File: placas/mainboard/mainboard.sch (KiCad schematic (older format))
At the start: 58 parts, among them IC1 DRV8843, K1 OjitoC1, K2 OjitoC2, K3 OjitoB1, K4 OjitoB2, K5 OjitoA1, K6 OjitoA2, P1 Bateria, P2 MI, P3 MD, P4 CONN_3X2, P5 CONN_3X2, P6 Solenoide, Q1 NPN, Q2 NPN, Q3 NPN, Q4 NPN, SW1 SW_PUSH_SMALL, U1 REG_104-5, U2 MBED

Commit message: transicion
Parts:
- added C? (x3): 4.7u, symbol CP
- added R? (x3): 100, symbol R
- C11, C12, C13: value 10u -> 4.7u
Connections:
- wire segments 255 -> 273
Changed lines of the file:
@@
-EESchema Schematic File Version 2  date jue 25 ago 2011 16:27:50 ART
+EESchema Schematic File Version 2  date jue 25 ago 2011 20:51:28 ART
 LIBS:power
 LIBS:device
@@
 $EndDescr
 Wire Wire Line
+	8850 2350 8450 2350
+Connection ~ 9900 1300
+Wire Wire Line
+	9900 1300 10350 1300
+Wire Wire Line
+	10350 1300 10350 1250
+Connection ~ 9900 700
+Wire Wire Line
+	9650 750  9650 700
+Wire Wire Line
+	9650 700  10100 700
+Wire Wire Line
+	9900 1250 9900 1600
+Connection ~ 9800 3100
+Wire Wire Line
+	9800 3100 10250 3100
+Wire Wire Line
+	10250 3100 10250 3050
+Wire Wire Line
+	9550 3400 9550 3050
+Connection ~ 9450 5100
+Wire Wire Line
+	9450 5100 10150 5100
+Wire Wire Line
+	10150 5100 10150 5200
+Connection ~ 9700 5600
+Wire Wire Line
+	9450 5550 9450 5600
+Wire Wire Line
+	9450 5600 9700 5600
+Wire Wire Line
+	9450 4800 9450 5150
+Wire Wire Line
 	6600 1250 6300 1250
 Wire Wire Line
@@
 	6600 2850 6300 2850
 Wire Wire Line
-	8750 2350 8450 2350
-Wire Wire Line
 	8750 1850 8450 1850
 Wire Wire Line
@@
 	8750 1250 8450 1250
 Wire Wire Line
-	850  5100 850  5250
+	850  5250 850  5100
 Wire Wire Line
 	3800 2250 4200 2250
@@
 Connection ~ 1450 1700
 Wire Wire Line
-	1450 1700 1450 1650
+	1450 1650 1450 1700
 Wire Wire Line
 	2300 1700 2300 2300
@@
 	9700 5650 9700 5550
 Wire Wire Line
-	9700 4800 9700 5150
-Wire Wire Line
-	9700 4300 9700 4250
-Wire Wire Line
-	9700 4250 9900 4250
-Wire Wire Line
-	9900 4250 9900 4300
+	9700 5150 9700 4800
+Wire Wire Line
+	9700 4250 9700 4300
+Wire Wire Line
+	9900 4300 9900 4250
 Wire Wire Line
 	9900 5400 10250 5400
 Connection ~ 9900 5000
 Wire Wire Line
-	10250 5200 10150 5200
+	10150 5200 10250 5200
 Connection ~ 10200 5300
 Wire Wire Line
@@
 Connection ~ 9800 4250
 Wire Wire Line
-	10150 5050 9700 5050
-Connection ~ 9700 5050
-Connection ~ 10150 5050
-Wire Wire Line
 	10200 4900 10200 5650
 Wire Wire Line
-	9250 5000 10250 5000
-Wire Wire Line
-	10150 4800 10150 5200
-Wire Wire Line
-	10250 3050 10250 3450
-Wire Wire Line
-	10350 3250 9350 3250
+	10250 5000 9050 5000
+Wire Wire Line
+	9150 3250 10350 3250
 Wire Wire Line
 	10300 3900 10300 3150
-Connection ~ 10250 3300
-Connection ~ 9800 3300
-Wire Wire Line
-	9800 3300 10250 3300
 Connection ~ 9900 2500
 Wire Wire Line
@@
 Connection ~ 10300 3550
 Wire Wire Line
-	10250 3450 10350 3450
+	10350 3450 10250 3450
 Connection ~ 10000 3250
 Wire Wire Line
@@
 Wire Wire Line
 	10000 2550 10000 2500
-Wire Wire Line
-	10000 2500 9800 2500
 Wire Wire Line
 	9800 2500 9800 2550
@@
 	9900 2100 9900 2000
 Wire Wire Line
-	9900 1250 9900 1600
-Wire Wire Line
-	9900 750  9900 700
-Wire Wire Line
-	10100 750  10100 700
+	9900 700  9900 750
+Wire Wire Line
+	10100 700  10100 750
 Wire Wire Line
 	10100 1850 10450 1850
@@
 Connection ~ 7650 5250
 Wire Wire Line
-	7650 5250 7650 5850
+	7650 5850 7650 5250
 Connection ~ 6500 4200
 Wire Wire Line
@@
 	6600 1550 6200 1550
 Wire Wire Line
-	800  3200 1150 3200
+	1150 3200 800  3200
 Wire Wire Line
 	3750 1550 4200 1550
@@
 	7050 4200 7050 4100
 Wire Wire Line
-	7550 5200 7550 5250
+	7550 5250 7550 5200
 Wire Wire Line
 	6100 5250 6100 5200
@@
 	7350 4200 7350 4250
 Wire Wire Line
-	6300 4200 6300 4250
+	6300 4250 6300 4200
 Wire Wire Line
 	3950 7350 3600 7350
@@
 Connection ~ 850  5150
 Wire Wire Line
-	850  5150 1400 5150
+	1400 5150 850  5150
 Connection ~ 850  6050
 Wire Wire Line
@@
 Connection ~ 4750 6400
 Wire Wire Line
-	4750 6500 4750 5250
-Wire Wire Line
-	3300 6400 4750 6400
-Wire Wire Line
-	4750 5600 3300 5600
+	4750 5250 4750 6500
+Wire Wire Line
+	4750 6400 3300 6400
+Wire Wire Line
+	3300 5600 4750 5600
 Wire Wire Line
 	4600 5150 4600 5250
@@
 	3950 7550 3600 7550
 Wire Wire Line
-	7550 4250 7550 4200
+	7550 4200 7550 4250
 Connection ~ 7550 4200
 Wire Wire Line
-	6300 5200 6300 5250
+	6300 5250 6300 5200
 Wire Wire Line
 	7350 5250 7350 5200
@@
 	8450 2150 8850 2150
 Wire Wire Line
-	1350 3400 1350 3750
-Wire Wire Line
-	10450 1250 10350 1250
+	1350 3750 1350 3400
+Wire Wire Line
+	10350 1250 10450 1250
 Wire Wire Line
 	4150 1350 4200 1350
@@
 	7300 5400 6800 5400
 Wire Wire Line
-	6400 5250 6400 5850
+	6400 5850 6400 5250
 Connection ~ 6400 5250
 Wire Wire Line
-	10000 700  10000 650
+	10000 650  10000 700
 Connection ~ 10000 700
 Wire Wire Line
-	10350 1500 9900 1500
-Connection ~ 9900 1500
-Connection ~ 10350 1500
-Wire Wire Line
 	10400 1350 10400 2100
 Wire Wire Line
-	9450 1450 10450 1450
+	10450 1450 9250 1450
 Wire Wire Line
 	2850 3800 2800 3800
@@
 Connection ~ 7050 4200
 Wire Wire Line
-	10350 1250 10350 1650
-Wire Wire Line
 	9200 6300 9550 6300
 Wire Wire Line
@@
 	8750 1050 8450 1050
 Wire Wire Line
-	10100 700  9900 700
-Wire Wire Line
 	8450 1150 8750 1150
 Wire Wire Line
@@
 Wire Wire Line
 	8450 1950 8750 1950
+Wire Wire Line
+	9450 4300 9450 4250
+Wire Wire Line
+	9450 4250 9900 4250
+Connection ~ 9700 4250
+Wire Wire Line
+	10150 4800 10150 4900
+Wire Wire Line
+	10150 4900 9700 4900
+Connection ~ 9700 4900
+Wire Wire Line
+	10000 2500 9550 2500
+Wire Wire Line
+	9550 2500 9550 2550
+Connection ~ 9800 2500
+Wire Wire Line
+	9800 3850 9550 3850
+Wire Wire Line
+	9550 3850 9550 3800
+Connection ~ 9800 3850
+Wire Wire Line
+	10250 3450 10250 3350
+Wire Wire Line
+	10250 3350 9550 3350
+Connection ~ 9550 3350
+Wire Wire Line
+	9650 2000 9650 2050
+Wire Wire Line
+	9650 2050 9900 2050
+Connection ~ 9900 2050
+Wire Wire Line
+	9650 1250 9650 1600
+Wire Wire Line
+	10350 1650 10350 1550
+Wire Wire Line
+	10350 1550 9650 1550
+Connection ~ 9650 1550
+$Comp
+L R R?
+U 1 1 4E56B7B3
+P 9650 1000
+F 0 "R?" V 9730 1000 50  0000 C CNN
+F 1 "100" V 9650 1000 50  0000 C CNN
+	1    9650 1000
+	1    0    0    -1
+$EndComp
+$Comp
+L CP C?
+U 1 1 4E56B7AB
+P 9650 1800
+F 0 "C?" H 9700 1900 50  0000 L CNN
+F 1 "4.7u" H 9700 1700 50  0000 L CNN
+	1    9650 1800
+	-1   0    0    -1
+$EndComp
+$Comp
+L R R?
+U 1 1 4E56B700
+P 9550 2800
+F 0 "R?" V 9630 2800 50  0000 C CNN
+F 1 "100" V 9550 2800 50  0000 C CNN
+	1    9550 2800
+	1    0    0    -1
+$EndComp
+$Comp
+L CP C?
+U 1 1 4E56B6FC
+P 9550 3600
+F 0 "C?" H 9600 3700 50  0000 L CNN
+F 1 "4.7u" H 9600 3500 50  0000 L CNN
+	1    9550 3600
+	-1   0    0    -1
+$EndComp
+$Comp
+L CP C?
+U 1 1 4E56B686
+P 9450 5350
+F 0 "C?" H 9500 5450 50  0000 L CNN
+F 1 "4.7u" H 9500 5250 50  0000 L CNN
+	1    9450 5350
+	-1   0    0    -1
+$EndComp
+$Comp
+L R R?
+U 1 1 4E56B682
+P 9450 4550
+F 0 "R?" V 9530 4550 50  0000 C CNN
+F 1 "100" V 9450 4550 50  0000 C CNN
+	1    9450 4550
+	1    0    0    -1
+$EndComp
 Text Label 8750 1050 2    60   ~ 0
 3v3
@@
 	1    0    0    1
 $EndComp
-Text Label 9250 5000 0    60   ~ 0
+Text Label 9050 5000 0    60   ~ 0
 OjitoC
 $Comp
@@
 P 9700 5350
 F 0 "C11" H 9750 5450 50  0000 L CNN
-F 1 "10u" H 9750 5250 50  0000 L CNN
+F 1 "4.7u" H 9750 5250 50  0000 L CNN
 	1    9700 5350
-	-1   0    0    -1
+	1    0    0    -1
 $EndComp
 $Comp
@@
 P 9800 3600
 F 0 "C12" H 9850 3700 50  0000 L CNN
-F 1 "10u" H 9850 3500 50  0000 L CNN
+F 1 "4.7u" H 9850 3500 50  0000 L CNN
 	1    9800 3600
-	-1   0    0    -1
+	1    0    0    -1
 $EndComp
 $Comp
@@
 	1    0    0    -1
 $EndComp
-Text Label 9350 3250 0    60   ~ 0
+Text Label 9150 3250 0    60   ~ 0
 OjitoB
-Text Label 9450 1450 0    60   ~ 0
+Text Label 9250 1450 0    60   ~ 0
 OjitoA
 Text Label 1900 3800 0    60   ~ 0
@@
 Text Label 8950 2850 2    60   ~ 0
 OjitosEmit1
-Text Label 6250 2250 0    60   ~ 0
+Text Label 8850 2050 2    60   ~ 0
 Puls
 Text Label 6200 1750 0    60   ~ 0
@@
 	1    0    0    -1
 $EndComp
-Text Label 8850 2050 2    60   ~ 0
+Text Label 8850 2150 2    60   ~ 0
 nReset
-Text Label 8850 2150 2    60   ~ 0
+Text Label 8850 2250 2    60   ~ 0
 nSleep
-Text Label 8850 2250 2    60   ~ 0
+Text Label 8850 2350 2    60   ~ 0
 nFault
 Text Label 8900 2750 2    60   ~ 0
@@
 P 9900 1800
 F 0 "C13" H 9950 1900 50  0000 L CNN
-F 1 "10u" H 9950 1700 50  0000 L CNN
+F 1 "4.7u" H 9950 1700 50  0000 L CNN
 	1    9900 1800
-	-1   0    0    -1
-$EndComp
-$Comp
+	1    0    0    -1
+$EndComp
+$Comp

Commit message: placa principal terminada
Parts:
- gave numbers to parts that had none: 6
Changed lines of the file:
@@
-EESchema Schematic File Version 2  date jue 25 ago 2011 20:51:28 ART
+EESchema Schematic File Version 2  date jue 25 ago 2011 20:52:22 ART
 LIBS:power
 LIBS:device
@@
 Connection ~ 9650 1550
 $Comp
-L R R?
+L R R6
 U 1 1 4E56B7B3
 P 9650 1000
-F 0 "R?" V 9730 1000 50  0000 C CNN
+F 0 "R6" V 9730 1000 50  0000 C CNN
 F 1 "100" V 9650 1000 50  0000 C CNN
 	1    9650 1000
@@
 $EndComp
 $Comp
-L CP C?
+L CP C16
 U 1 1 4E56B7AB
 P 9650 1800
-F 0 "C?" H 9700 1900 50  0000 L CNN
+F 0 "C16" H 9700 1900 50  0000 L CNN
 F 1 "4.7u" H 9700 1700 50  0000 L CNN
 	1    9650 1800
@@
 $EndComp
 $Comp
-L R R?
+L R R5
 U 1 1 4E56B700
 P 9550 2800
-F 0 "R?" V 9630 2800 50  0000 C CNN
+F 0 "R5" V 9630 2800 50  0000 C CNN
 F 1 "100" V 9550 2800 50  0000 C CNN
 	1    9550 2800
@@
 $EndComp
 $Comp
-L CP C?
+L CP C15
 U 1 1 4E56B6FC
 P 9550 3600
-F 0 "C?" H 9600 3700 50  0000 L CNN
+F 0 "C15" H 9600 3700 50  0000 L CNN
 F 1 "4.7u" H 9600 3500 50  0000 L CNN
 	1    9550 3600
@@
 $EndComp
 $Comp
-L CP C?
+L CP C14
 U 1 1 4E56B686
 P 9450 5350
-F 0 "C?" H 9500 5450 50  0000 L CNN
+F 0 "C14" H 9500 5450 50  0000 L CNN
 F 1 "4.7u" H 9500 5250 50  0000 L CNN
 	1    9450 5350
@@
 $EndComp
 $Comp
-L R R?
+L R R4
 U 1 1 4E56B682
 P 9450 4550
-F 0 "R?" V 9530 4550 50  0000 C CNN
+F 0 "R4" V 9530 4550 50  0000 C CNN
 F 1 "100" V 9450 4550 50  0000 C CNN
 	1    9450 4550

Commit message: retoques finales
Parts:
- added P7: CONN_1, symbol CONN_1
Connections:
- wire segments 273 -> 275

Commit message: cambios en el puente h, reubicacion de componentes en la placa
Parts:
- removed C1: 100n, symbol C
- removed IC1: DRV8843, HTSSOP28, symbol DRV8843
- removed R1, R2: 10k, symbol R
- added C1: 2.2u, symbol CP
- added IC1: DRV8833, symbol DRV8833
- added JP1: JUMPER, symbol JUMPER
- added P8: CONN_1, symbol CONN_1
- C9: value 100u -> 10u
- R10, R11, R13, R14, R15, R9: value 220 -> 2k2
- R12, R8: value 1k -> 10k
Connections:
- net labels removed: nReset
- wire segments 275 -> 236
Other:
- moved on the sheet: C10, C7, C8, C9, P2, P3, P4, P5, P7, Q1, R3

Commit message: nueva version de la placa mainboard
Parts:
- removed C11, C12, C13, C14, C15: 4.7u, symbol CP
- removed D2, D3, D4, D5: LED, symbol LED
- removed K1: OjitoC1, symbol CONN_3
- removed K2: OjitoC2, symbol CONN_3
- removed K3: OjitoB1, symbol CONN_3
- removed K4: OjitoB2, symbol CONN_3
- removed K5: OjitoA1, symbol CONN_3
- removed R10, R11, R13, R14: 2k2, symbol R
- removed R17, R18, R19, R4, R5: 100, symbol R
- removed R20, R21: 4.7k, symbol R
- added C_OJ2: 4.7u, symbol CP
- added C_UC1: 100n, symbol C
- added IC_UC1: ATMEGA88PA-P, DIL28, symbol ATMEGA88PA-P
- added K_OJ2: OjitoATR, symbol CONN_3
- added P1, P2: CONN_1, symbol CONN_1
- added P_UC1: CONN_3X2, symbol CONN_3X2
- added P_UC2: CONN_4, symbol CONN_4
- added R_OJ4: 4.7k, symbol R
- added R_OJ8: 100, symbol R
- added R_UC1: 10k, symbol R
- added SW_UC1: SW_PUSH_SMALL, symbol SW_PUSH_SMALL
- K_OJ1: renamed from K6; value OjitoA2 -> OjitoAD
- renumbered C2 to C_B1, C4 to C_B2, C5 to C_B3, C6 to C_B4, C16 to C_OJ1, C8 to C_PH1, C1 to C_PH2, C7 to C_PH3, C9 to C_PH4, C10 to C_PH5, C3 to C_Pl1, D1 to D_OJ1, D6 to D_OJ2, D7 to D_SL1, IC1 to IC_PH1, U2 to IC_UC2, JP1 to JP_B1, P7 to P3, P8 to P4, P1 to P_B1, P4 to P_E1, P5 to P_E2, P2 to P_PH1, P3 to P_PH2, P6 to P_SL1, Q1 to Q_E1, Q2 to Q_OJ1, Q3 to Q_OJ2, Q4 to Q_SL1, R3 to R_E1, R8 to R_OJ1, R9 to R_OJ2, R22 to R_OJ3, R15 to R_OJ5, R12 to R_OJ6, R6 to R_OJ7, R16 to R_SL1, SW1 to SW_Pl1, U1 to U_B1
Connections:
- net labels added: ATMISO, ATMOSI, ATRESET, ATRX, ATSCK, ATTX, OjitoRecepAd, OjitoRecepAtr, OjitosEmitAd, OjitosEmitAtr
- net labels removed: OjitoA, OjitoB, OjitoC, OjitosEmit1, OjitosEmit2
- wire segments 236 -> 238
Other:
- moved on the sheet: C_OJ1, D_OJ1, D_OJ2, D_SL1, K_OJ1, P3, P_PH1, P_PH2, P_SL1, Q_OJ1, Q_OJ2, Q_SL1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

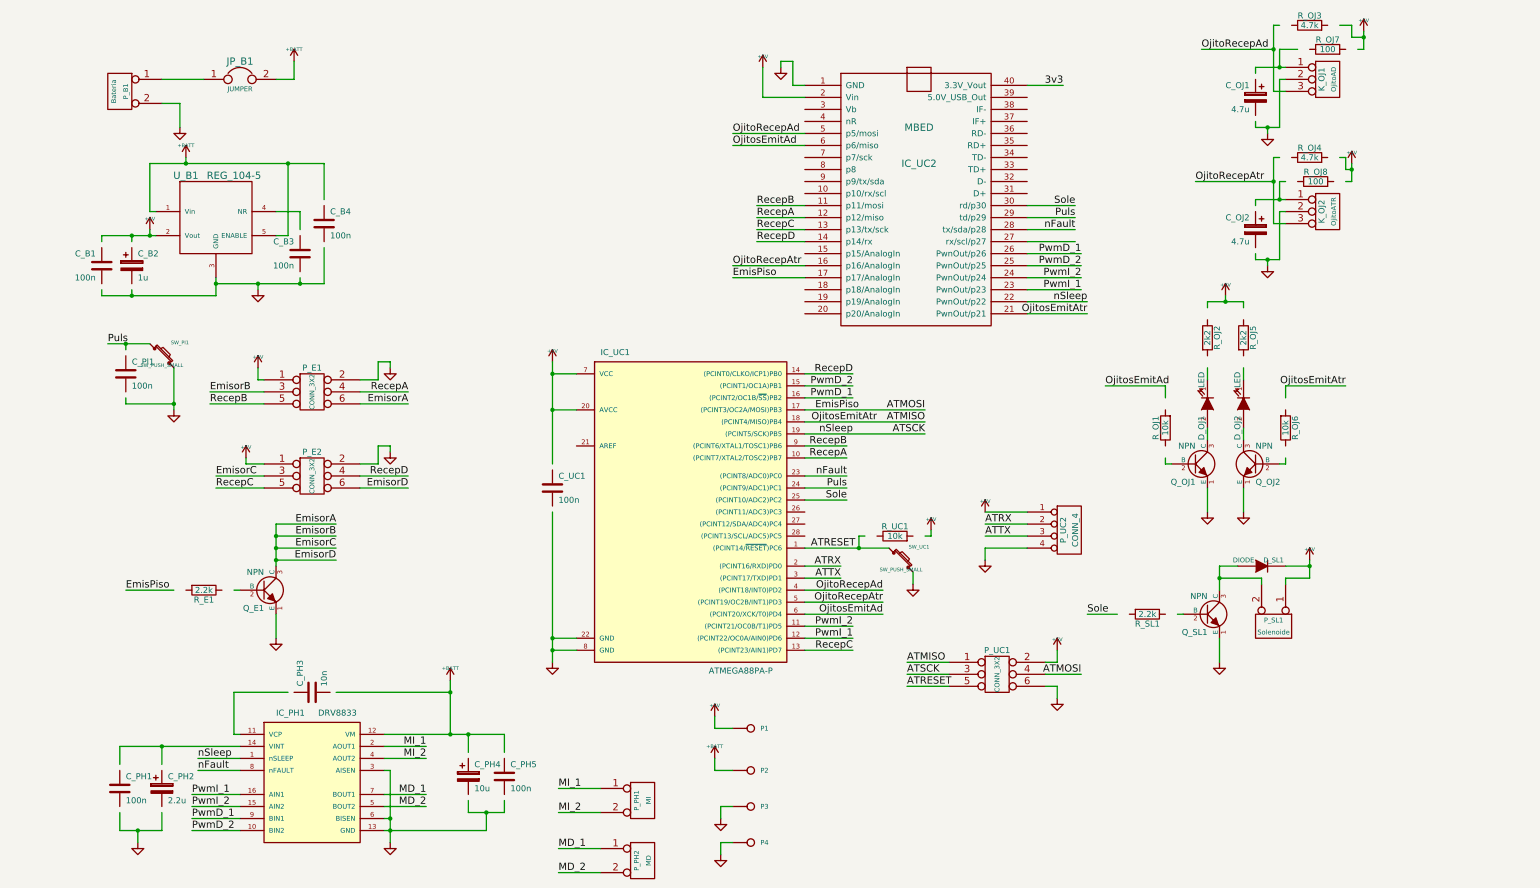
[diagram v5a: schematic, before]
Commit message: reposicionamos un receptor del piso y eliminamos el receptor infrarrojo trasero
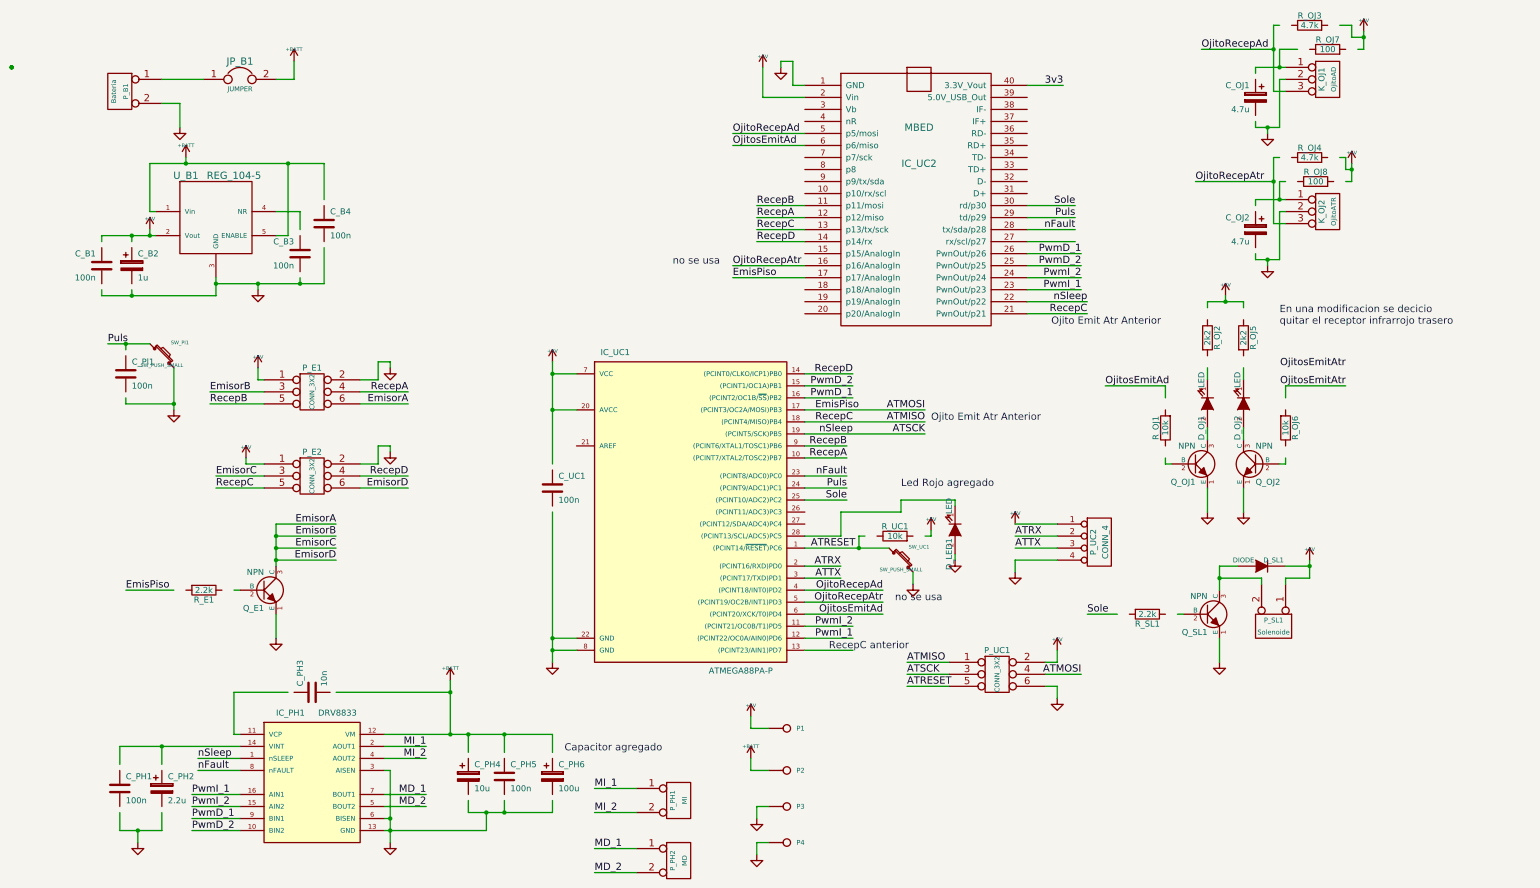
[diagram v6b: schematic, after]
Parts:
- added C_PH6: 100u, symbol CP
- added D_LED1: LED, symbol LED
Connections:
- wire segments 238 -> 247
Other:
- note added: "Capacitor agregado"
- note added: "En una modificacion se decicio\nquitar el receptor infrarrojo trasero"
- note added: "Led Rojo agregado"
- note added: "Ojito Emit Atr Anterior"
- note added: "RecepC anterior"
- note added: "no se usa"
- moved on the sheet: P1, P2, P3, P4, P_PH1, P_PH2, P_UC2

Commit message: actualizo las placas con las modificaciones hechas
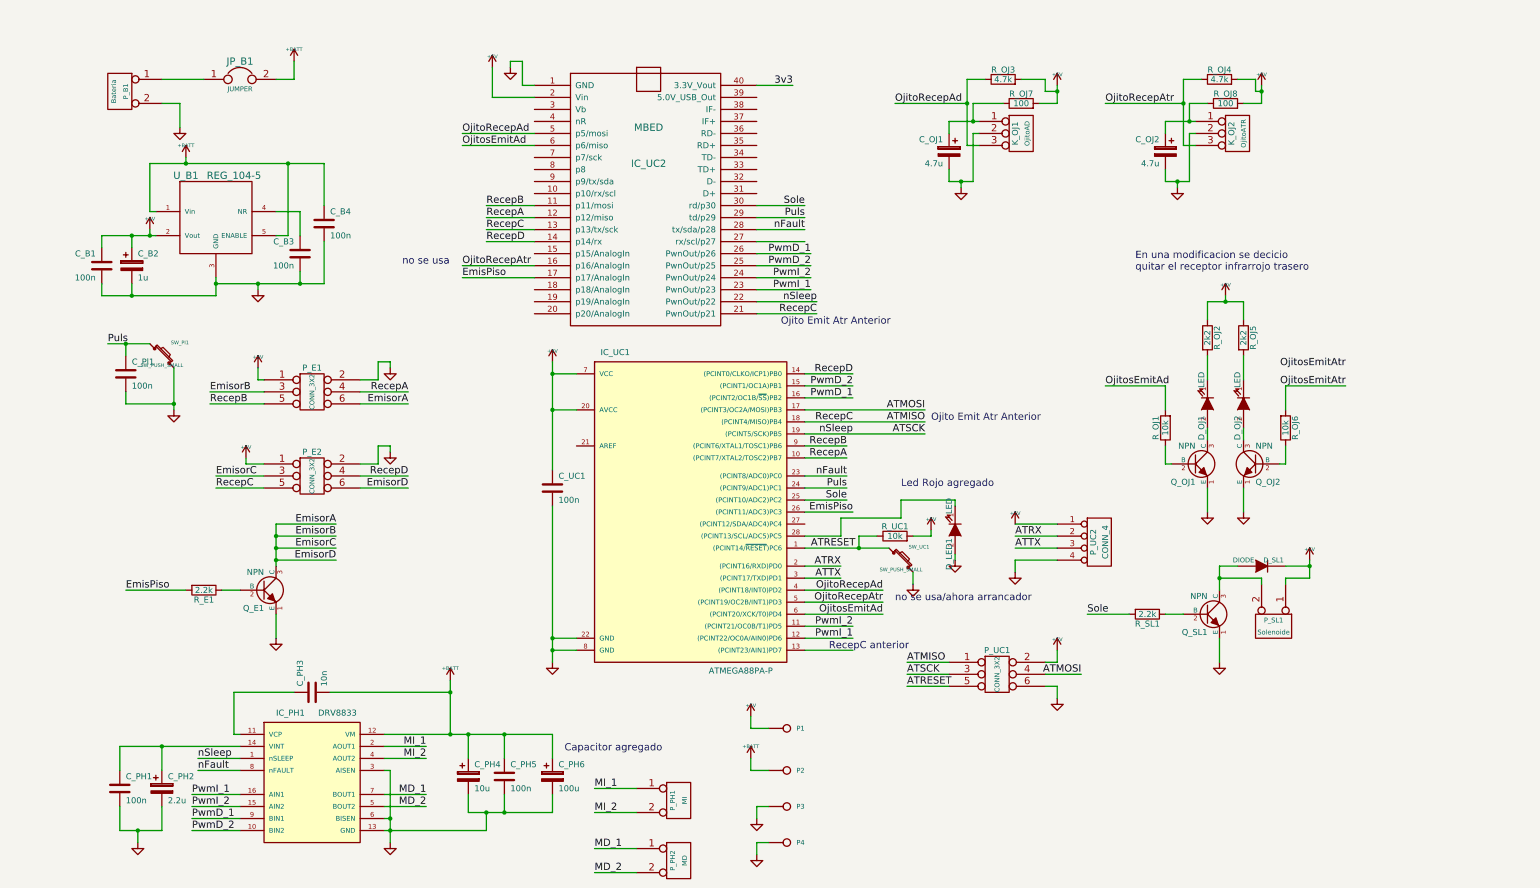
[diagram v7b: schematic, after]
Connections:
- wire segments 247 -> 248
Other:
- note added: "no se usa/ahora arrancador"
- moved on the sheet: C_OJ1, C_OJ2, IC_UC2, K_OJ1, K_OJ2, R_OJ3, R_OJ4, R_OJ7, R_OJ8
